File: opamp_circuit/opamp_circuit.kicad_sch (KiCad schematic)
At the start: 49 parts, among them J1 INP, J2 INM, J3 Vout, J4 VDD, J5 VSS, J6 Vref, J7 Vref_out, J8 GND, U1 OPA846xDBV, U2 OPA846xDBV, U3 AD8429ARZ

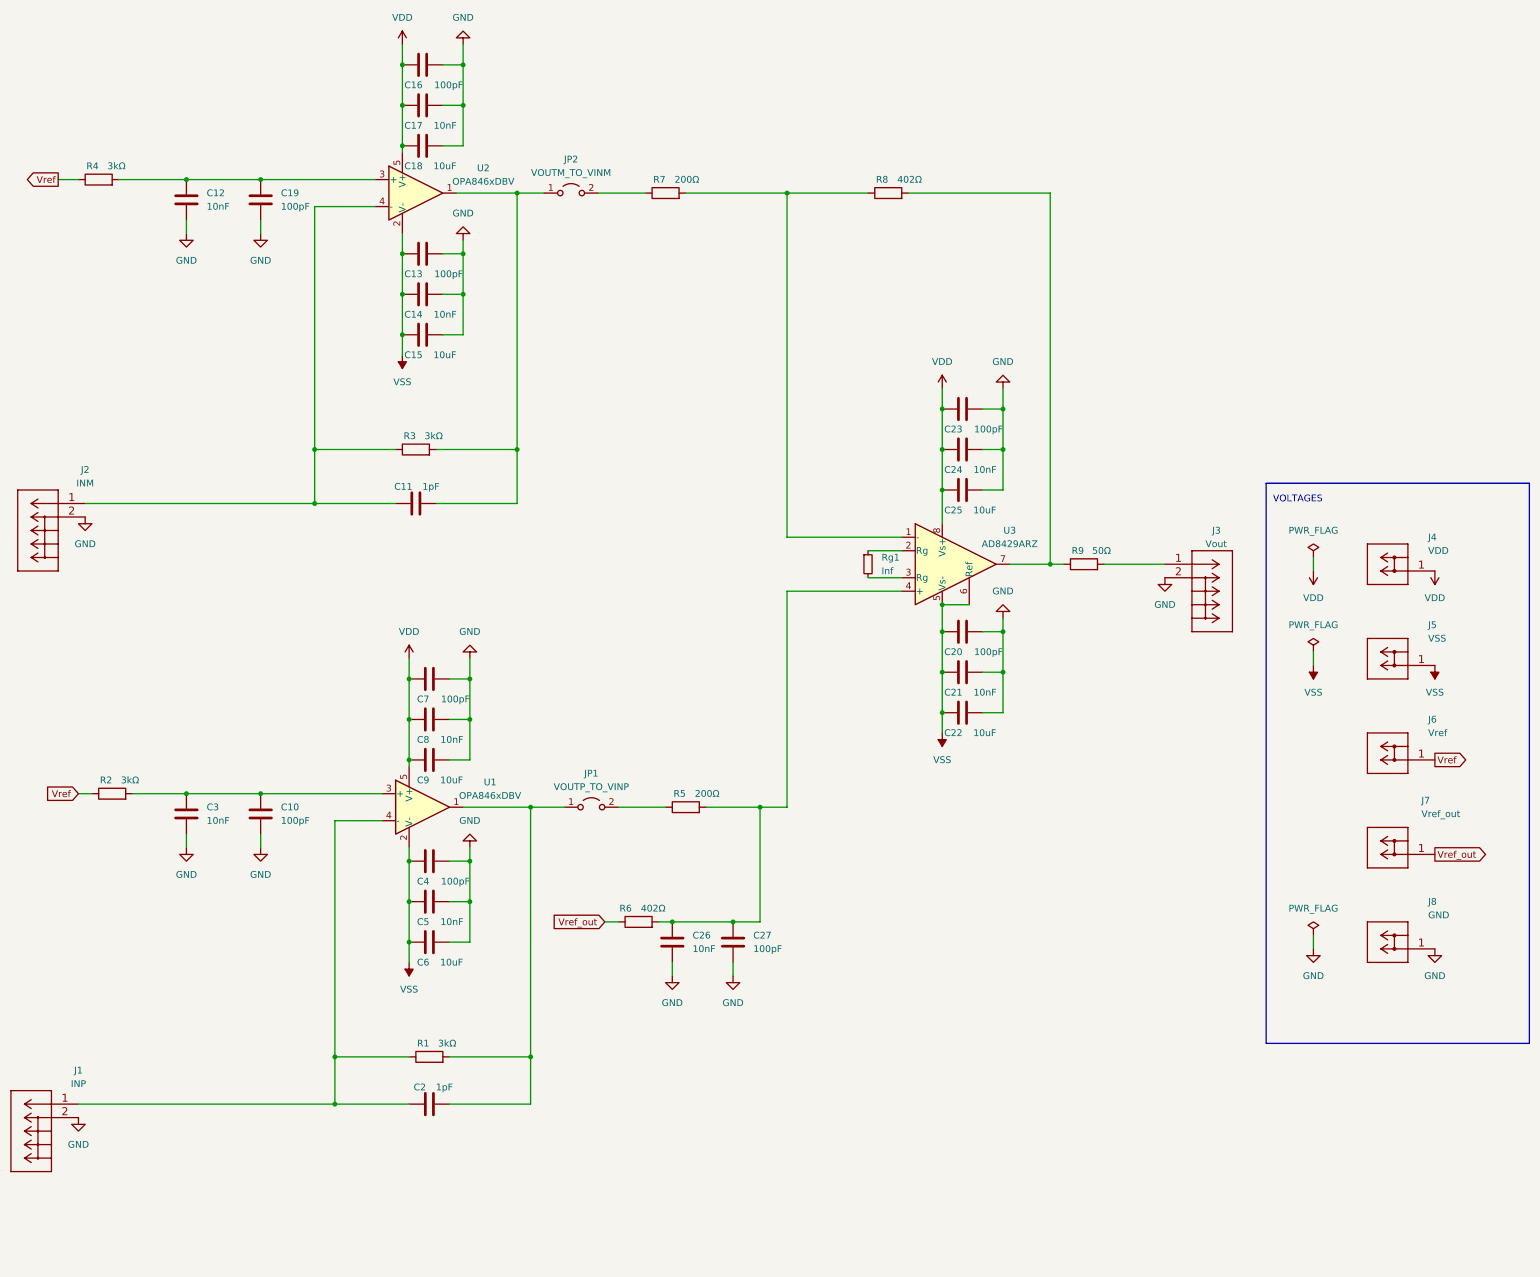
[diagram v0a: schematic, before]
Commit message: Better placement and uniform capa, redesign adapting to the instrumentation opamp
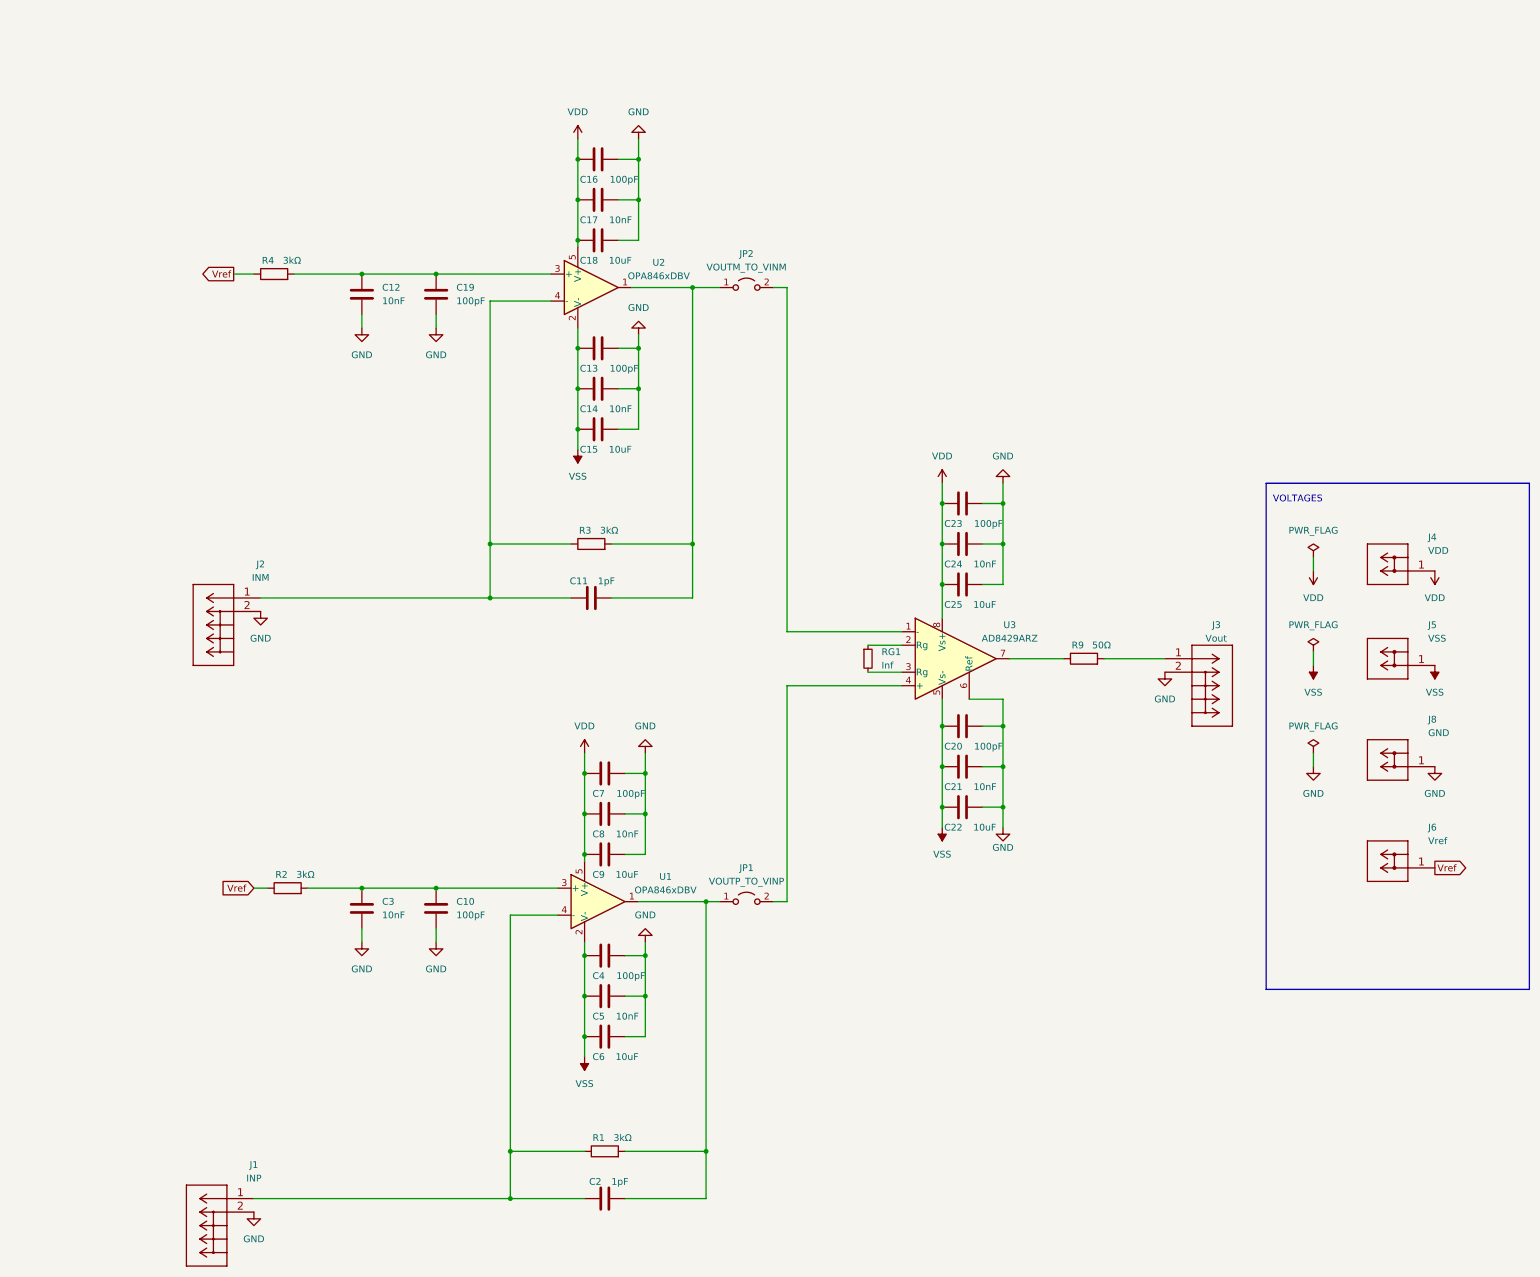
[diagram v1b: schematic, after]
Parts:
- removed C26: 10nF, created_lib:06035C103JAT2A, symbol Device:C
- removed C27: 100pF, created_lib:CL05C101JB5NNNC, symbol Device:C
- removed J7: Vref_out, created_lib:973582101, symbol created_lib:973582101
- removed R5, R7: 200Ω, Resistor_SMD:R_0603_1608Metric, symbol Device:R
- removed R6, R8: 402Ω, Resistor_SMD:R_0603_1608Metric, symbol Device:R
- C10, C13, C16, C19, C20, C23, C4, C7: footprint created_lib:CL05C101JB5NNNC -> Capacitor_SMD:C_1206_3216Metric; Shop link https://www.digikey.ch/en/products/detail/samsung-electro-m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 -> https://www.digikey.ch/en/products/detail/kyocera-avx/12061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
- C11, C2: footprint created_lib:CC1206JRNPO9BN102 -> Capacitor_SMD:C_1206_3216Metric
- C12, C14, C17, C21, C24, C3, C5, C8: footprint created_lib:06035C103JAT2A -> Capacitor_SMD:C_1206_3216Metric; Shop link https://www.digikey.ch/en/products/detail/kyocera-avx/06035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 -> https://www.digikey.ch/en/products/detail/kyocera-avx/12063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
- R1, R2, R3, R4: footprint Resistor_SMD:R_0402_1005Metric -> Resistor_SMD:R_1206_3216Metric_Pad1.30x1.75mm_HandSolder; Shop link https://www.digikey.ch/en/products/detail/susumu/RR0510P-30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 -> https://www.digikey.ch/en/products/detail/yageo/RC1206FR-07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
- RG1: renamed from Rg1; footprint Resistor_SMD:R_0805_2012Metric_Pad1.20x1.40mm_HandSolder -> Resistor_SMD:R_1206_3216Metric_Pad1.30x1.75mm_HandSolder
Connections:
- net GND: now also U3.6 (Ref)
- net VSS: no longer U3.6 (Ref)
- net at JP2.2 (B): now also U3.1 (-)
- net at U3.4 (+): now also JP1.2 (B)
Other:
- moved on the sheet: C10, C11, C12, C13, C14, C15, C16, C17, C18, C19, C2, C20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

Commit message: Renamed capa
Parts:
- renumbered C2 to C1, C7 to C10, C8 to C11, C9 to C12, C20 to C19, C3 to C2, C21 to C20, C22 to C21, C23 to C22, C24 to C23, C25 to C24, C10 to C3, C11 to C4, C12 to C5, C19 to C6, C4 to C7, C5 to C8, C6 to C9, J6 to J4, J4 to J5, J5 to J6, J8 to J7, R9 to R5
